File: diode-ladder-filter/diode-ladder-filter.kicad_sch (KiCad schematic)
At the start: 72 parts, among them J1 Input, J10 Input, J11 Output, J12 Conn_01x04_Socket, J13 Conn_01x04_Pin, J2 CV1, J3 CV2, J4 Output, J5 Power, J6 Power, J8 CV1, J9 CV2, SW1 LPF, SW2 Resonance_safety, SW3 BPF, SW4 HPF, U1 TL074, U2 TL074

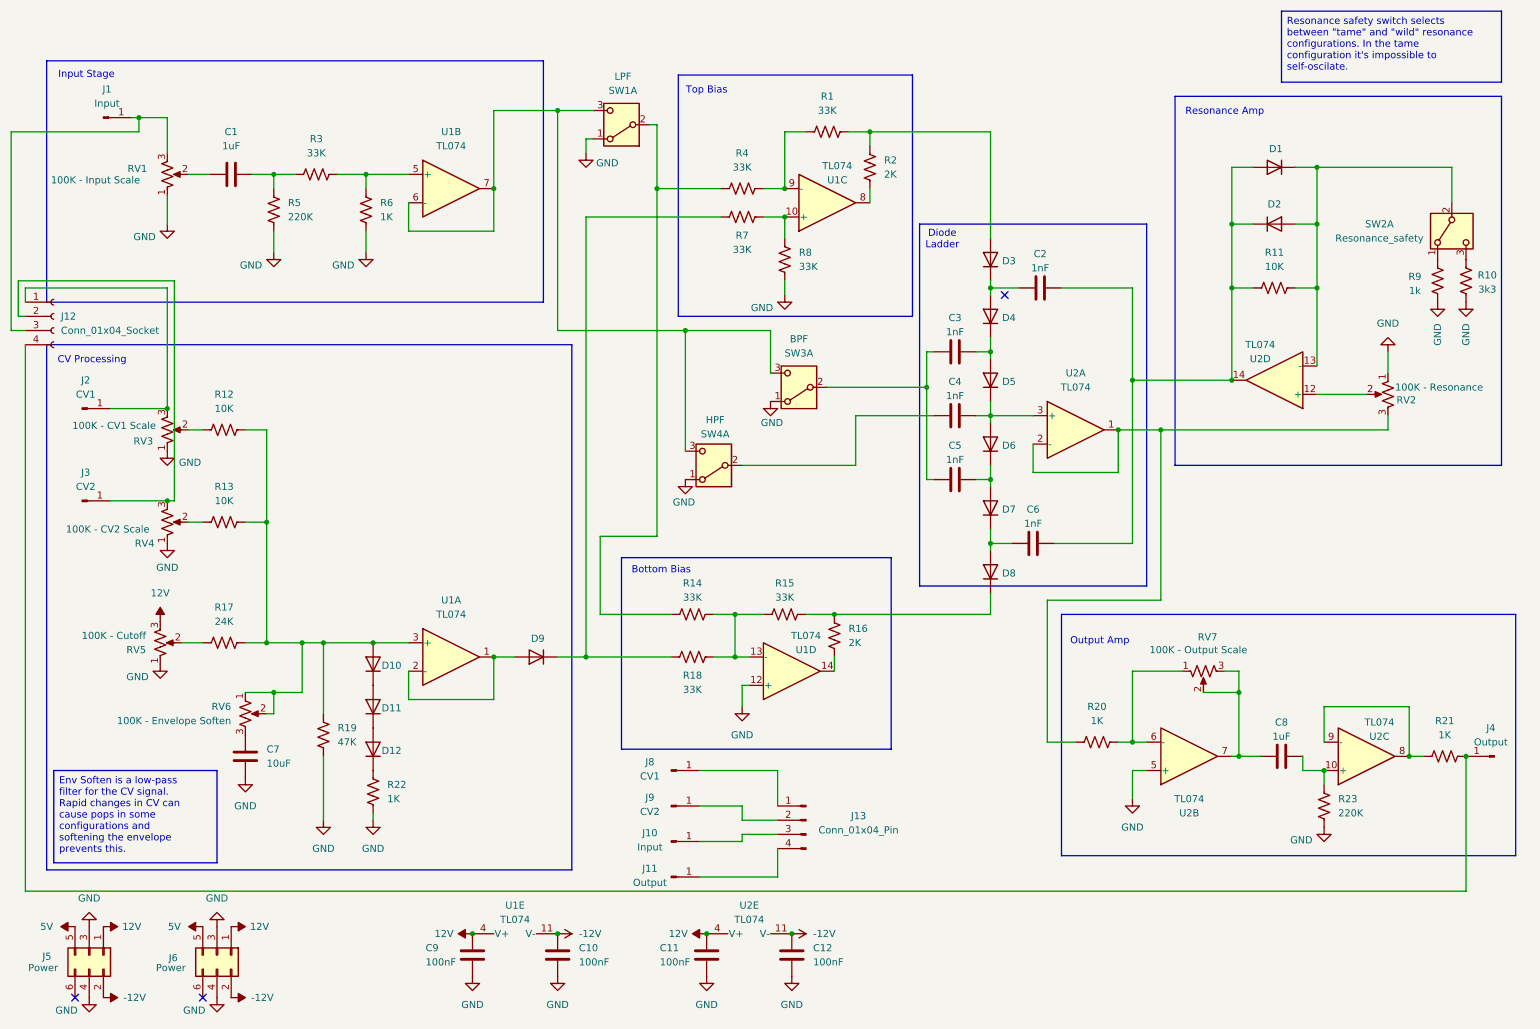
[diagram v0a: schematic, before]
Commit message: Renumber some components
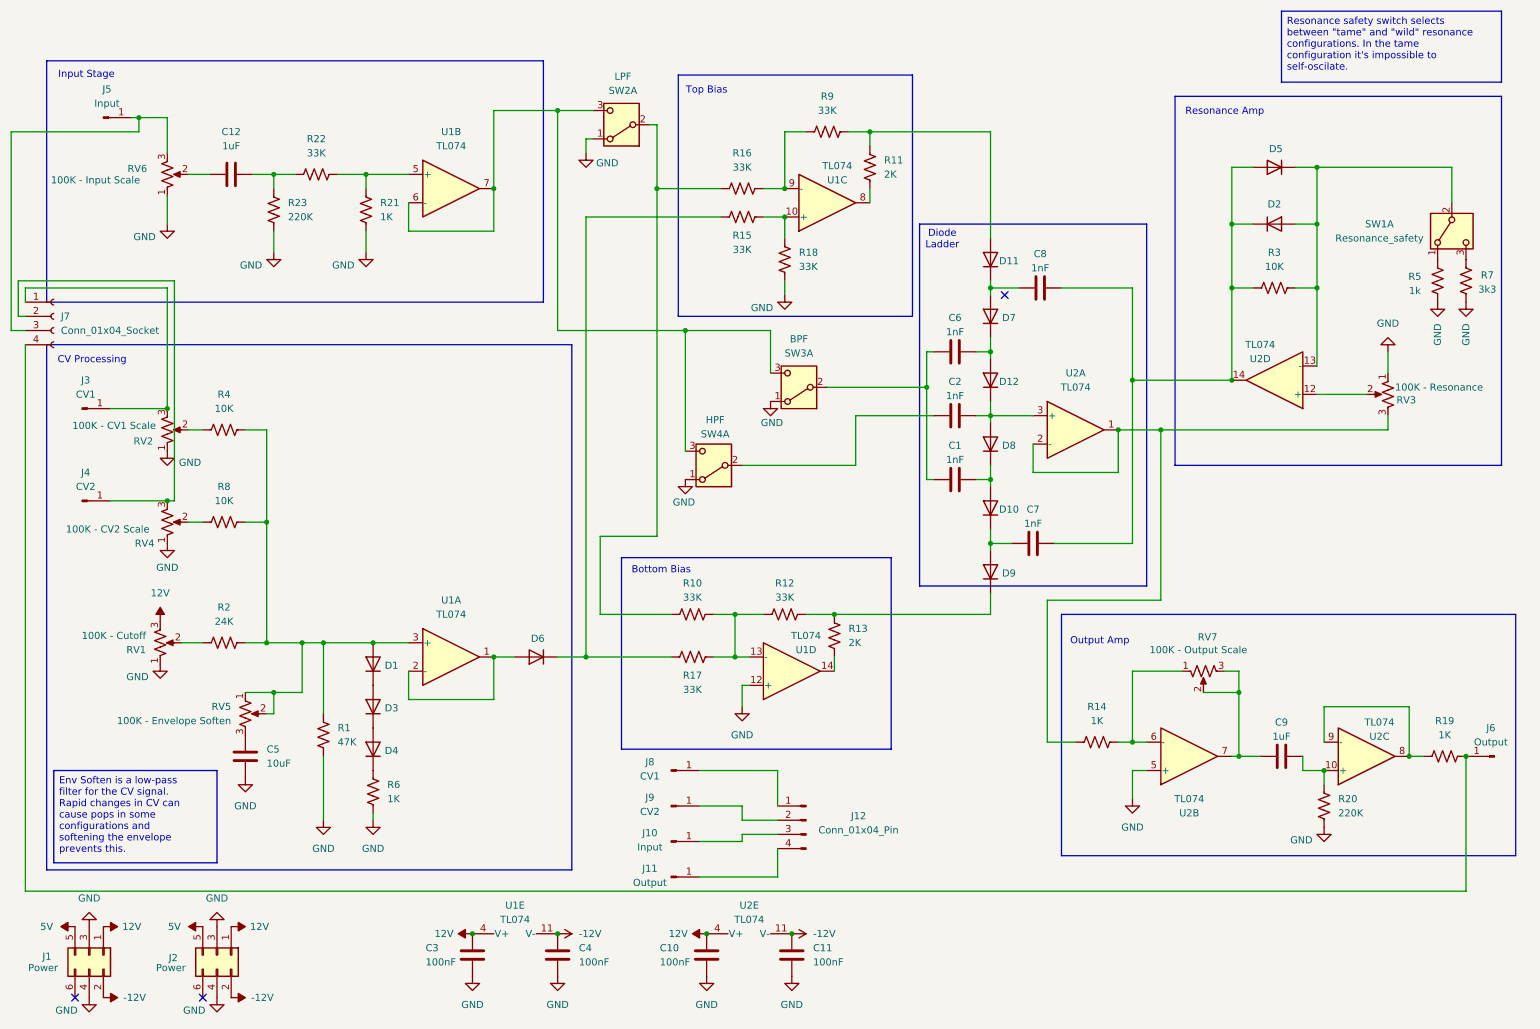
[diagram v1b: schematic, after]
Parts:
- renumbered C5 to C1, C11 to C10, C12 to C11, C1 to C12, C4 to C2, C9 to C3, C10 to C4, C7 to C5, C3 to C6, C6 to C7, C2 to C8, C8 to C9, D10 to D1, D7 to D10, D3 to D11, D5 to D12, D11 to D3, D12 to D4, D1 to D5, D9 to D6, D4 to D7, D6 to D8, D8 to D9, J5 to J1, J13 to J12, J6 to J2, J2 to J3, J3 to J4, J1 to J5, J4 to J6, J12 to J7, R19 to R1, R14 to R10, R2 to R11, R15 to R12, R16 to R13, R20 to R14, R7 to R15, R4 to R16, R18 to R17, R8 to R18, R21 to R19, R17 to R2, R23 to R20, R6 to R21, R3 to R22, R5 to R23, R11 to R3, R12 to R4, R9 to R5, R22 to R6, R10 to R7, R13 to R8, R1 to R9, RV5 to RV1, RV3 to RV2, RV2 to RV3, RV6 to RV5, RV1 to RV6, SW2 to SW1, SW1 to SW2

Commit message: Revert "Renumber some components"
This reverts commit 4c9a93e4336de2276d9b49e02718b6a92f997a6a.
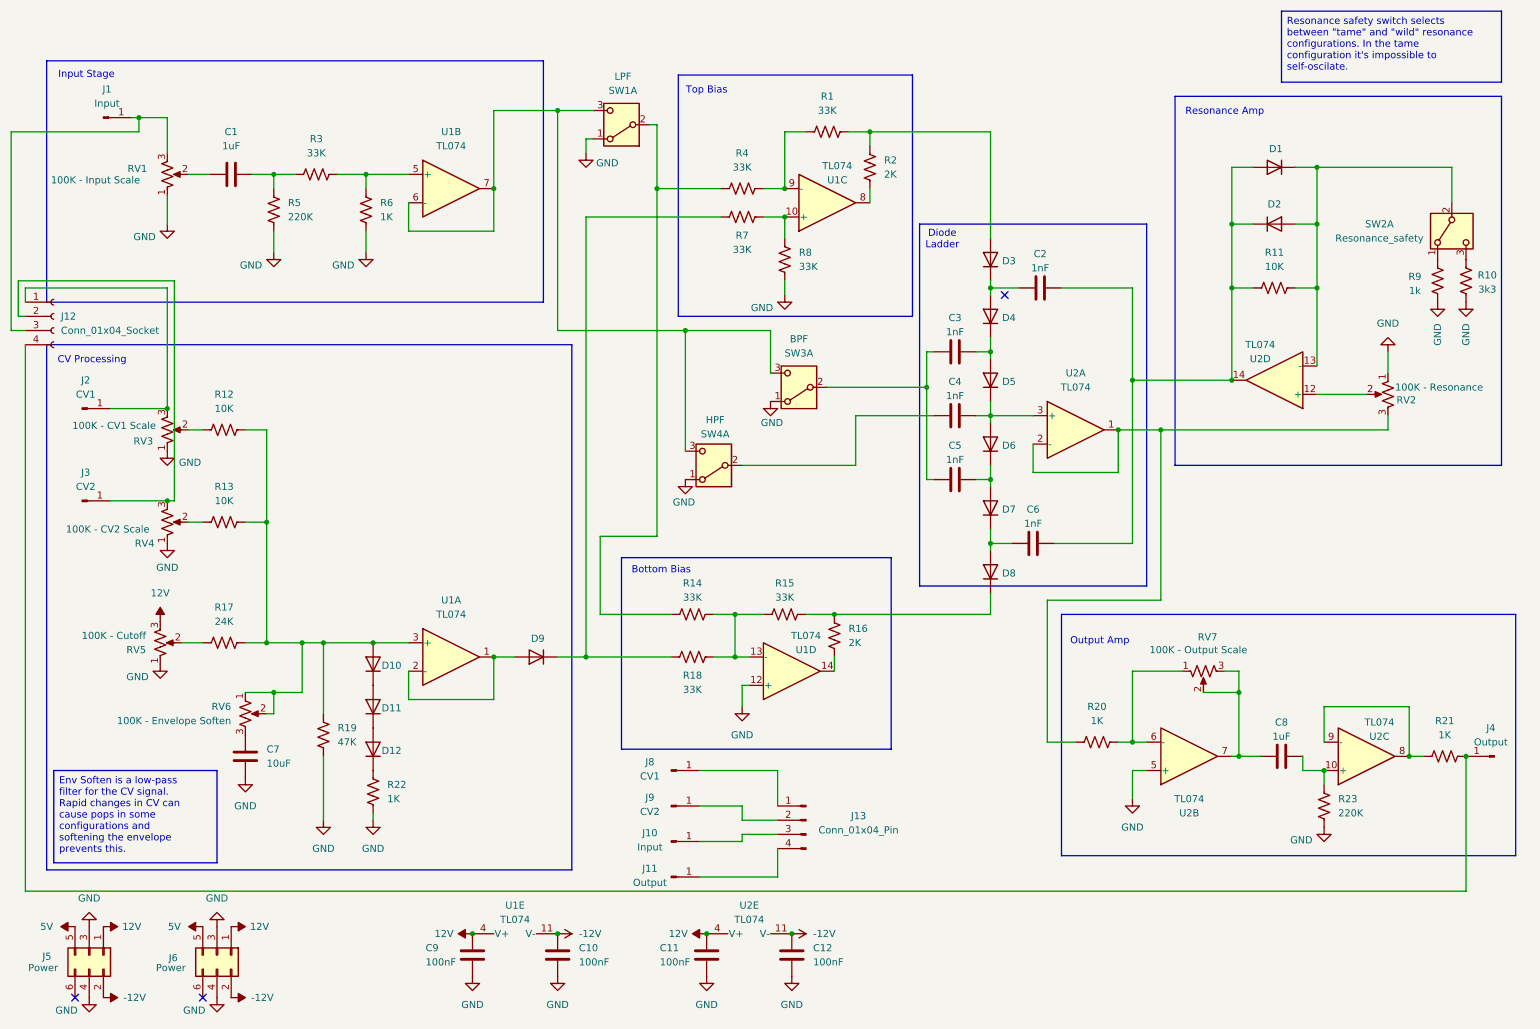
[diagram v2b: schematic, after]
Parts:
- renumbered C12 to C1, C4 to C10, C10 to C11, C11 to C12, C8 to C2, C6 to C3, C2 to C4, C1 to C5, C7 to C6, C5 to C7, C9 to C8, C3 to C9, D5 to D1, D1 to D10, D3 to D11, D4 to D12, D11 to D3, D7 to D4, D12 to D5, D8 to D6, D10 to D7, D9 to D8, D6 to D9, J5 to J1, J7 to J12, J12 to J13, J3 to J2, J4 to J3, J6 to J4, J1 to J5, J2 to J6, R9 to R1, R7 to R10, R3 to R11, R4 to R12, R8 to R13, R10 to R14, R12 to R15, R13 to R16, R2 to R17, R17 to R18, R1 to R19, R11 to R2, R14 to R20, R19 to R21, R6 to R22, R20 to R23, R22 to R3, R16 to R4, R23 to R5, R21 to R6, R15 to R7, R18 to R8, R5 to R9, RV6 to RV1, RV3 to RV2, RV2 to RV3, RV1 to RV5, RV5 to RV6, SW2 to SW1, SW1 to SW2
